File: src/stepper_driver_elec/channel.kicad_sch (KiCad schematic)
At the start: 39 parts, among them J1 VH4, U2 DMHT6016LFJ, U3 DMHT6016LFJ, U4 TMC5160A-TA

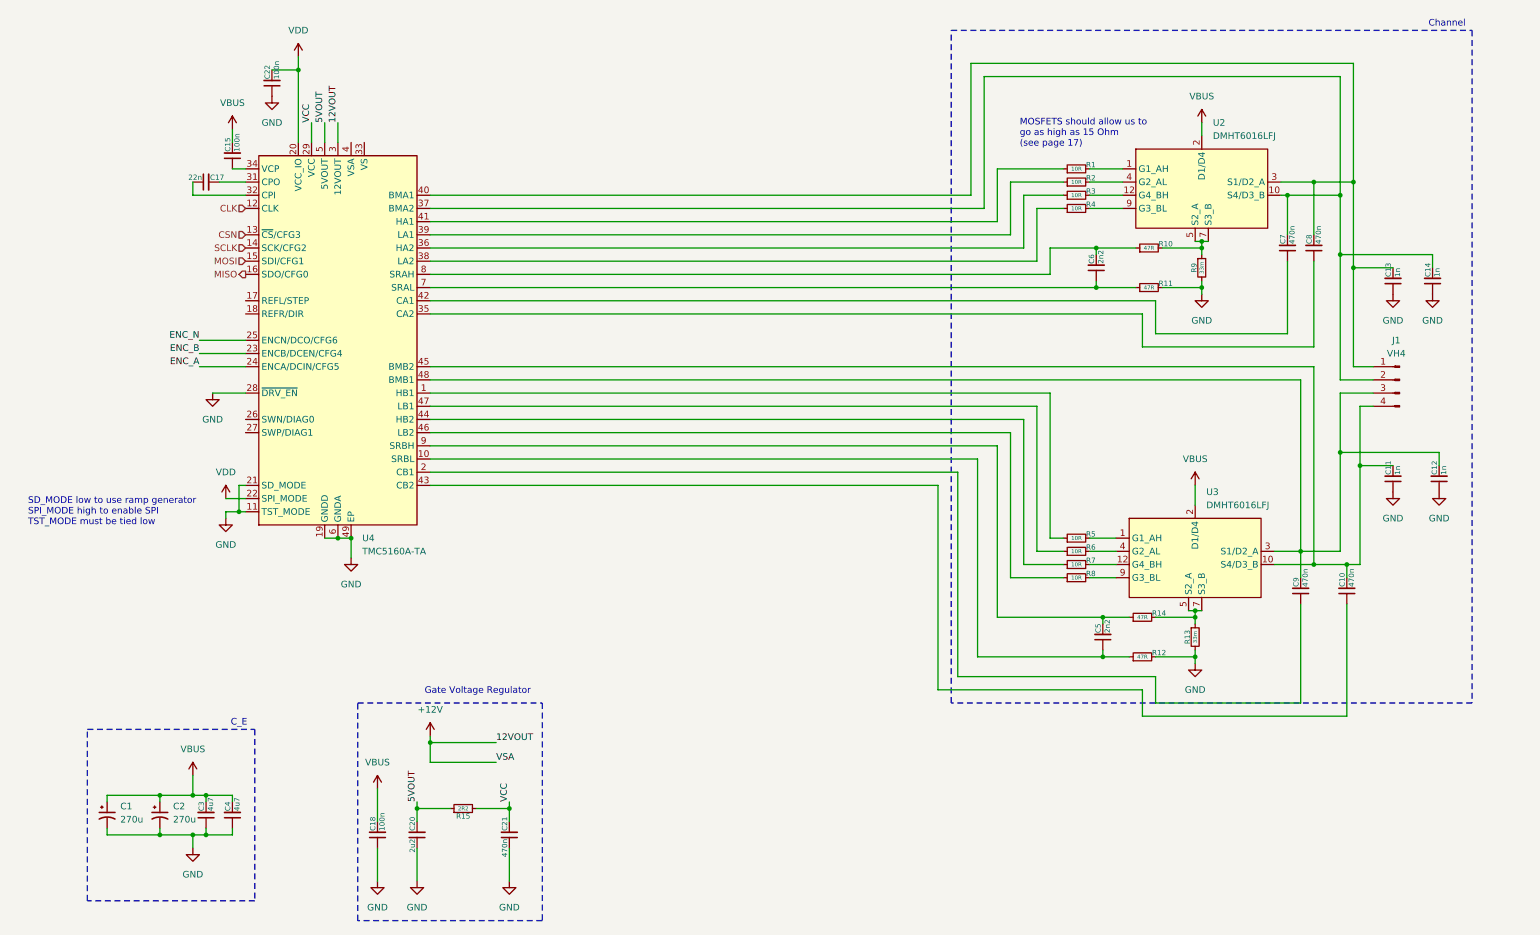
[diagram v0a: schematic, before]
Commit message: Add documentation for choices and capacitor specs
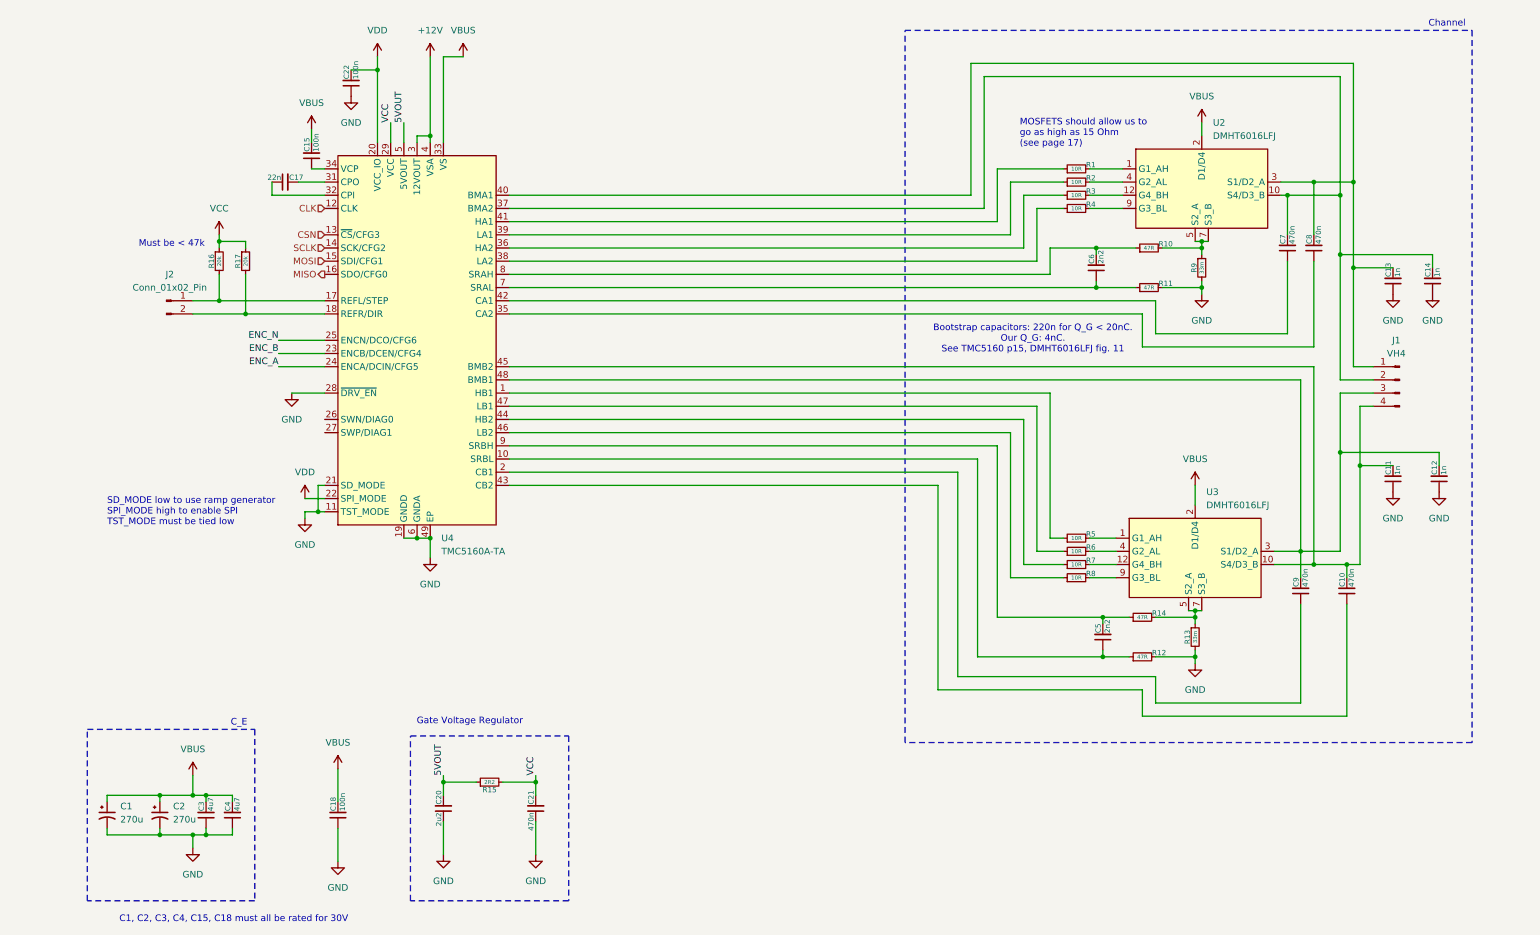
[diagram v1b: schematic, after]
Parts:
- added J2: Conn_01x02_Pin, symbol Connector:Conn_01x02_Pin
- added R16, R17: 20k, symbol Bluesat:R_CompactV
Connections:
- net +12V: now also U4.4 (VSA)
- net D1/D4: now also U4.33 (VS)
- net VCC: now also R16.1, R17.1
- net at U4.17 (REFL/STEP): now also J2.1 (Pin_1), R16.2
- net at U4.18 (REFR/DIR): now also J2.2 (Pin_2), R17.2
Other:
- note added: "Bootstrap capacitors: 220n for Q_G < 20nC. Our Q_G: 4nC. See TMC5160 p15, DMHT6016LFJ fig. 11"
- note added: "C1, C2, C3, C4, C15, C18 must all be rated for 30V"
- note added: "Must be < 47k"
- moved on the sheet: C15, C17, C18, C20, C21, C22, R15, U4

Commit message: Add net labels, fix certain layout things to be clearer
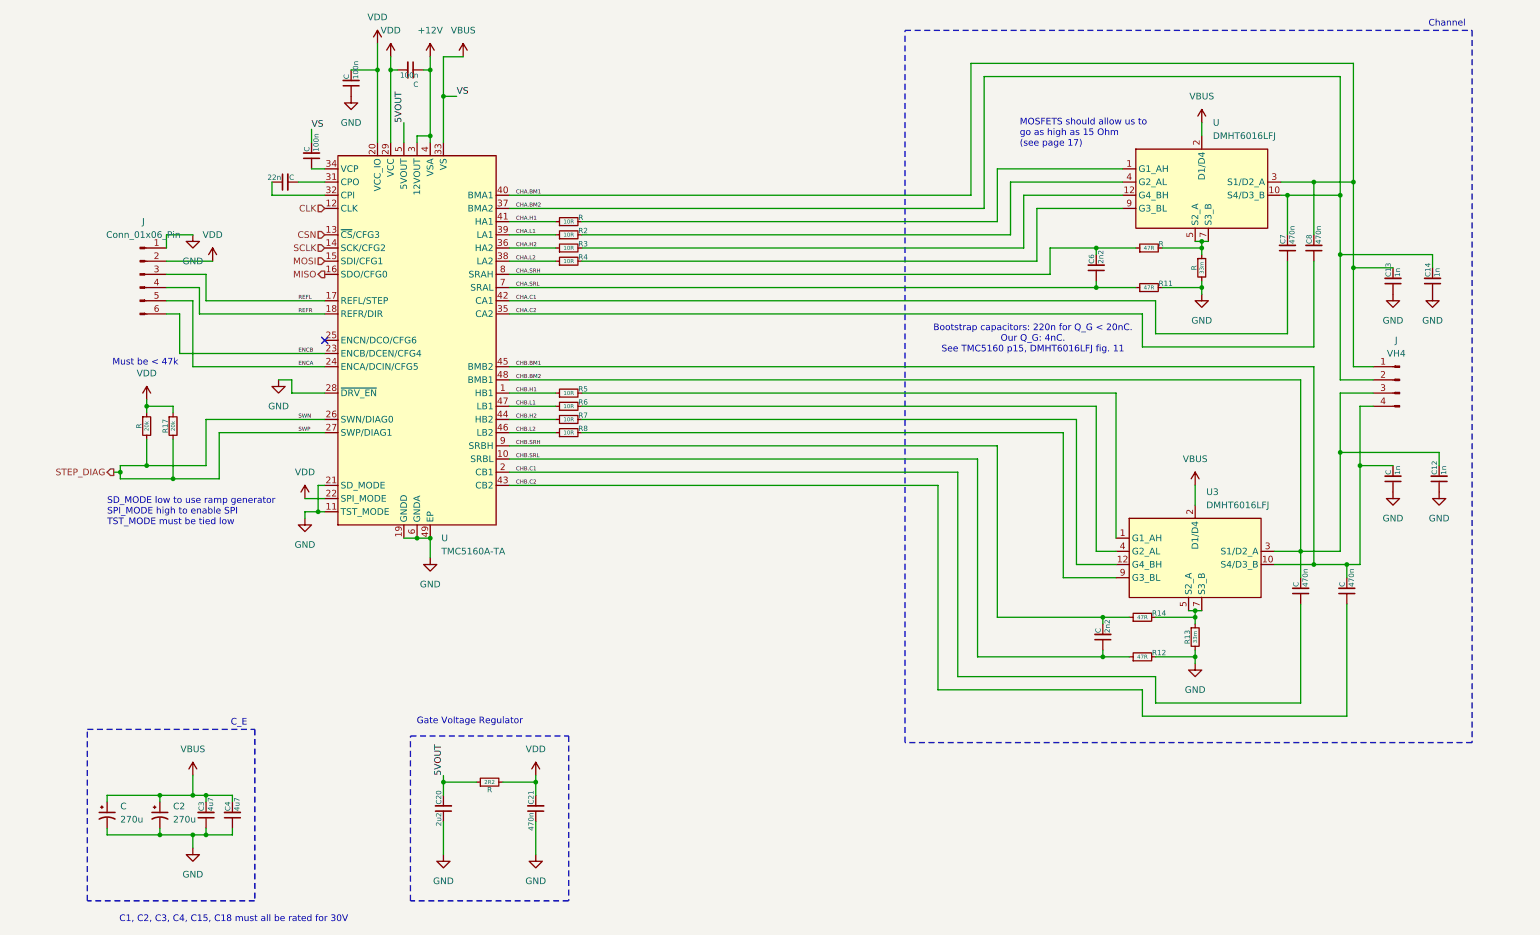
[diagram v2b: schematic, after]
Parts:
- removed J2: Conn_01x02_Pin, symbol Connector:Conn_01x02_Pin
- added J: Conn_01x06_Pin, symbol Connector:Conn_01x06_Pin
- renumbered C10 to C, C9 to C, C1 to C, C17 to C, C18 to C, C22 to C, C11 to C, C15 to C, C5 to C, J1 to J, R16 to R, R9 to R, R10 to R, R15 to R, R1 to R, U2 to U, U4 to U
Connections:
- net VCC is gone; now on net VDD: C21.2, R.1, R.2, R17.1, U.29 (VCC)
- net +12V: now also C.1
- net D1/D4: no longer C.2
- net GND: now also J.1 (Pin_1); no longer C.1
- net VDD: now also C.2, J.2 (Pin_2)
- net CHB.C2: now reaches C.1, U.43 (CB2)
- net CHB.BM1: now reaches C.2, C.2, J.4 (Pin_4), U.45 (BMB2), U3.10 (S4/D3_B)
- net CHA.SRL: now reaches C6.1, R11.1, U.7 (SRAL)
- net CHB.BM2: now reaches C.2, C12.2, J.3 (Pin_3), U.48 (BMB1), U3.3 (S1/D2_A)
- net CHB.H2: now reaches R7.1, U.44 (HB2)
- net CHB.C1: now reaches C.1, U.2 (CB1)
- net REFL: now reaches U.17 (REFL/STEP)
- net REFL: now also J.3 (Pin_3); no longer R.2
- net REFR: now reaches U.18 (REFR/DIR)
- net REFR: now also J.4 (Pin_4); no longer R17.2
- net CHB.L1: now reaches R6.1, U.47 (LB1)
- net CHA.L2: now reaches R4.1, U.38 (LA2)
- net CHA.SRH: now reaches C6.2, R.1, U.8 (SRAH)
- net CHB.H1: now reaches R5.1, U.1 (HB1)
- net CHA.H2: now reaches R3.1, U.36 (HA2)
- net CHA.BM2: now reaches C14.2, C7.2, J.2 (Pin_2), U.10 (S4/D3_B), U.37 (BMA2)
- net CHA.BM1: now reaches C13.2, C8.2, J.1 (Pin_1), U.3 (S1/D2_A), U.40 (BMA1)
- net CHA.C1: now reaches C7.1, U.42 (CA1)
- net CHB.SRL: now reaches C.1, R12.1, U.10 (SRBL)
- net STEP_DIAG: now reaches U.26 (SWN/DIAG0)
- net STEP_DIAG: now also R.2, R17.2, U.27 (SWP/DIAG1)
- net CHA.C2: now reaches C8.1, U.35 (CA2)
- net CHA.L1: now reaches R2.1, U.39 (LA1)
- net CHA.H1: now reaches R.1, U.41 (HA1)
- net CHB.L2: now reaches R8.1, U.46 (LB2)
- net CHB.SRH: now reaches C.2, R14.1, U.9 (SRBH)
- net ENC_A renamed ENCA
- net ENCA: now also J.5 (Pin_5)
- net ENC_B renamed ENCB
- net ENCB: now also J.6 (Pin_6)
- net ENC_N: no longer names the net of U.25 (ENCN/DCO/CFG6)
- no-connect marks 0 -> 1
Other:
- moved on the sheet: C, R, R17, R2, R3, R4, R5, R6, R7, R8

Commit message: Add TVS Diodes (no sex component yet 😔)
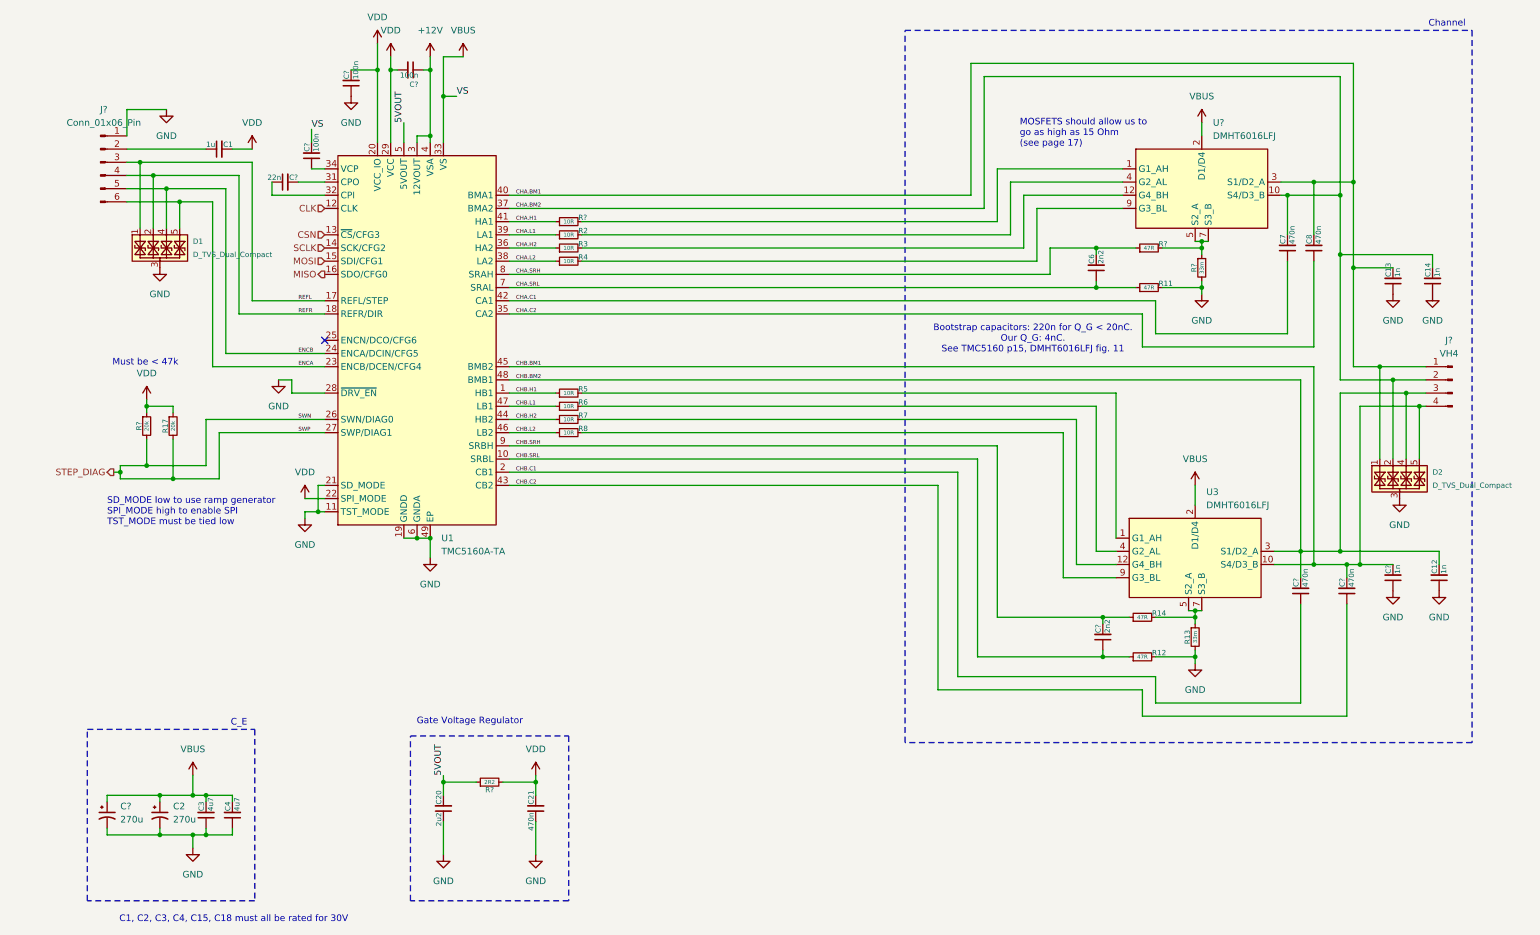
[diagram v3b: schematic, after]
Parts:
- added C1: 1u, symbol Bluesat:C_CompactH
- added D1, D2: D_TVS_Dual_Compact, symbol Bluesat:D_TVS_Quad_Compact
- renumbered C to C?, J to J?, R to R?, U to U1, U to U?
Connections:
- net CHA.BM1: now also D2.1, D2.10
- net CHA.BM2: now also D2.2, D2.9
- net CHB.BM1: now also D2.5, D2.6
- net CHB.BM2: now also D2.4, D2.7
- net ENCA: now also J?.6 (Pin_6), U1.23 (ENCB/DCEN/CFG4), D1.5, D1.6; no longer J?.5 (Pin_5), U1.24 (ENCA/DCIN/CFG5)
- net ENCB: now also J?.5 (Pin_5), U1.24 (ENCA/DCIN/CFG5), D1.4, D1.7; no longer J?.6 (Pin_6), U1.23 (ENCB/DCEN/CFG4)
- net GND: now also D1.3, D1.8, D2.3, D2.8
- net REFL: now also D1.1, D1.10
- net REFR: now also D1.2, D1.9
- net VDD: now also C1.2; no longer J?.2 (Pin_2)
- new net: C1.1, J?.2 (Pin_2)
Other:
- moved on the sheet: C12, C?, J?

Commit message: Put channels on NEN, add ARGB & Thermistor
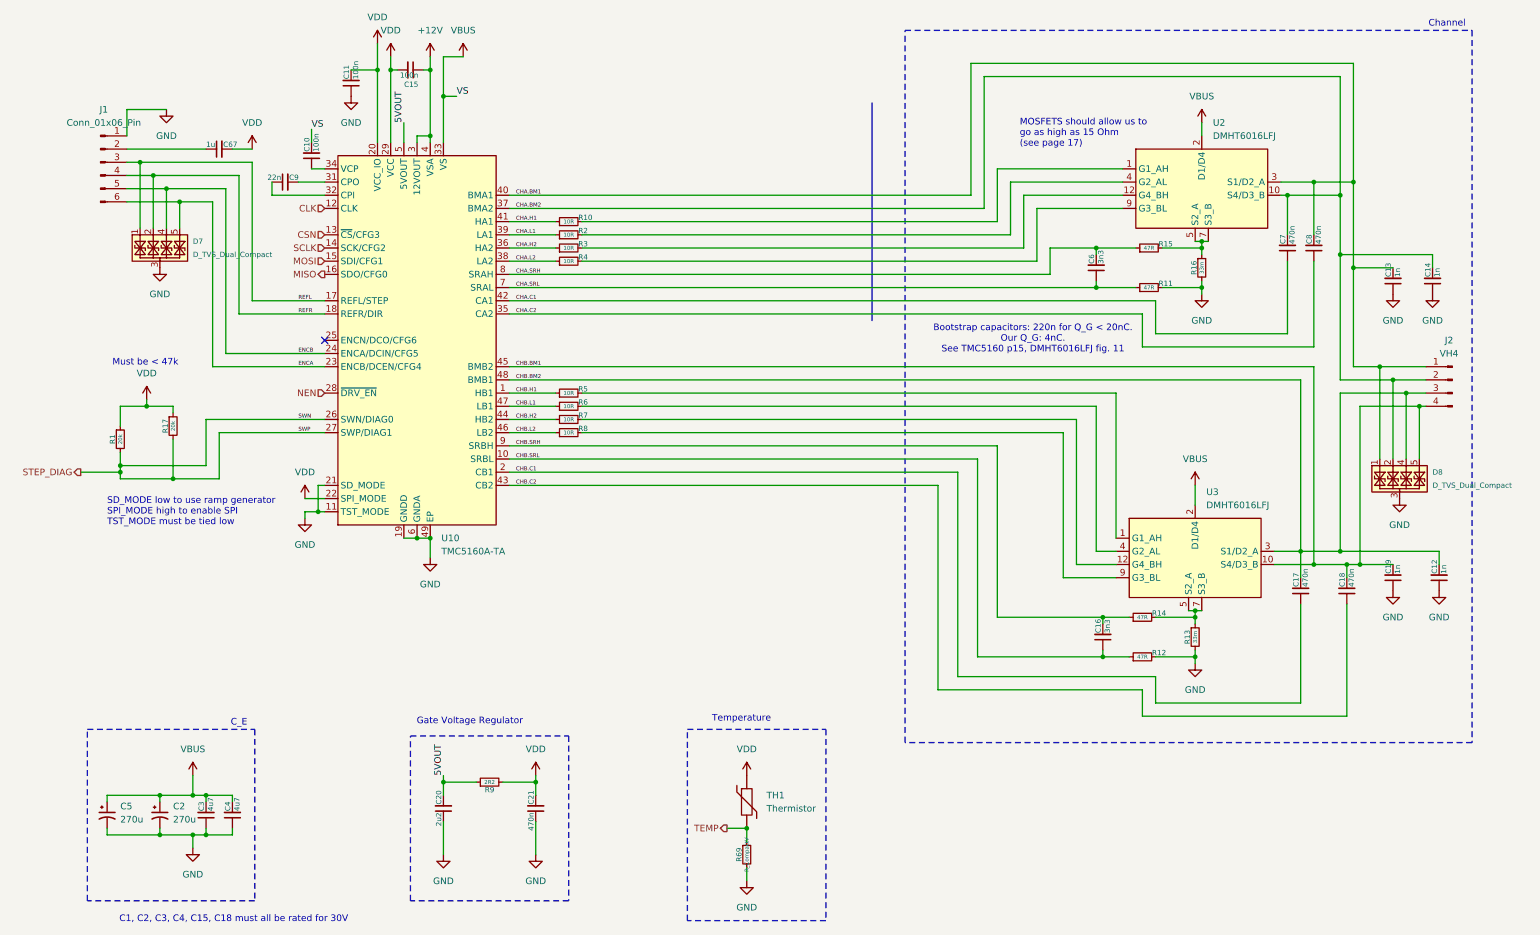
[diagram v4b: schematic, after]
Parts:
- added R69: R_CompactV, symbol Bluesat:R_CompactV
- added TH1: Thermistor, symbol Device:Thermistor
- C16: renamed from C?; value 2n2 -> 3n3
- C6: value 2n2 -> 3n3
- gave numbers to parts that had none: 16
- renumbered C1 to C67, D1 to D7, D2 to D8, U1 to U10
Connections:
- net GND: now also R69.2; no longer U10.28 (~{DRV_EN})
- net VDD: now also TH1.1
- new net NEN: U10.28 (~{DRV_EN})
- new net TEMP: R69.1, TH1.2
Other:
- note added: "Temperature"
- moved on the sheet: R1

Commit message: Add RC BW calculation
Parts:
- R69: value R_CompactV -> 10k
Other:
- note added: "BW=1/(47R*2 * 3n3 * 2π=513 Hz"
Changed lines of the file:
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@@
 		)
 	)
+	(text "BW=1/(47R*2 * 3n3 * 2π=513 Hz"
+		(exclude_from_sim no)
+		(at 210.058 65.024 0)
+		(effects
+			(font
+				(size 0.762 0.762)
+			)
+		)
+	)
 	(text "Temperature"
 		(exclude_from_sim no)
@@
 			)
 		)
-		(property "Value" "R_CompactV"
+		(property "Value" "10k"
 			(at 142.24 176.53 90)
 			(do_not_autoplace yes)
